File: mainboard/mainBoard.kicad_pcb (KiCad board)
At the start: 4 copper layers, 109.8 x 59.1 mm, 87 parts, among them IC1 TCAN3414DR, J1 XT60PW-M, J10 XT30U-M, J11 XT30U-M, J12 CAN Connector, J13 B2B-PH-K, J14 B2B-PH-K, J15 B2B-PH-K, J16 BM04B-SRSS-TB, J2 XT60PW-M, J20 BM04B-SRSS-TB, J21 B2B-PH_K, J22 Conn_01x02, J23 Jertson Header, J24 B2B-PH-K, J25 B2B-PH-K, J26 B2B-PH-K, J3 XT30PW-M, J4 XT30PW-M, J6 XT30U_M, J7 XT30U-M, J8 XT30U-M, J9 XT30U-M, Q1 FQD11P06TM, Q2 FQD11P06TM, U1 TPS565208, U2 TPS565208

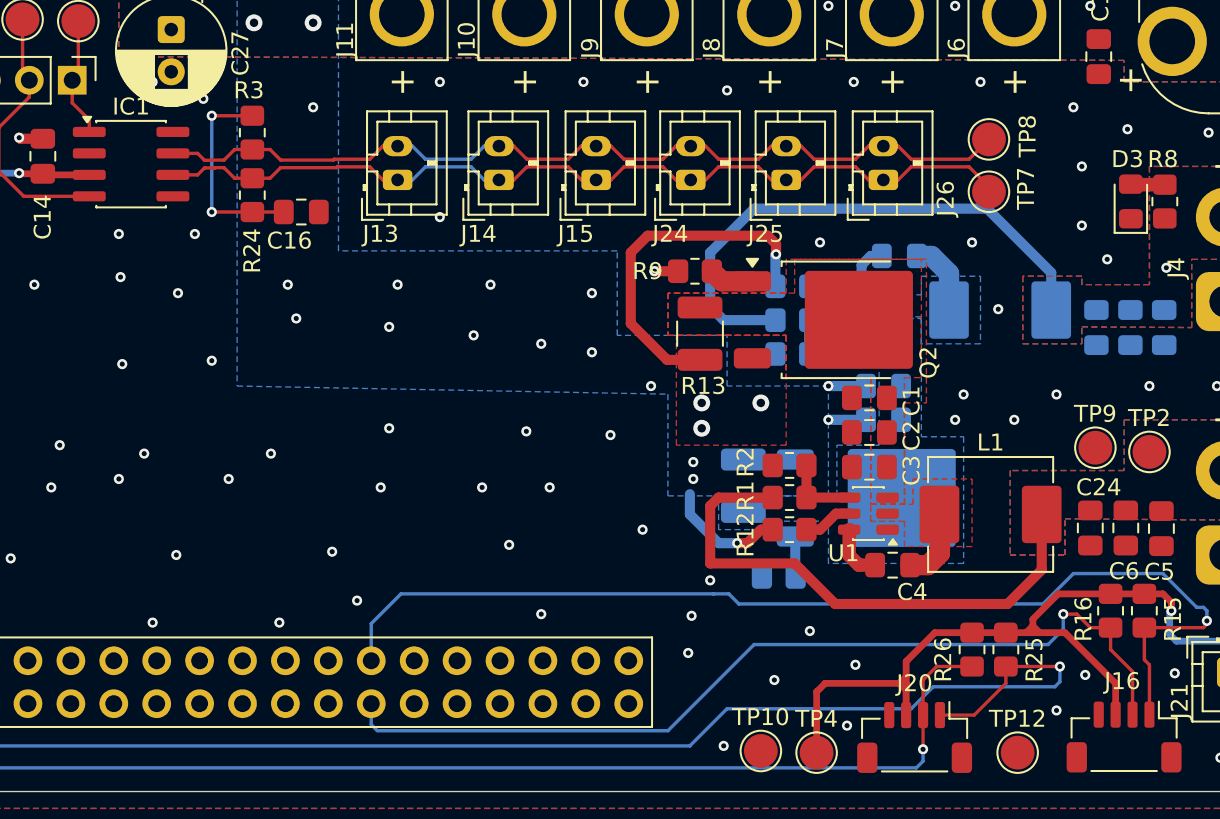
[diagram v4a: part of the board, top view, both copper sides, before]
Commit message: added tvs diode to baord (this was sylvester not nitin)
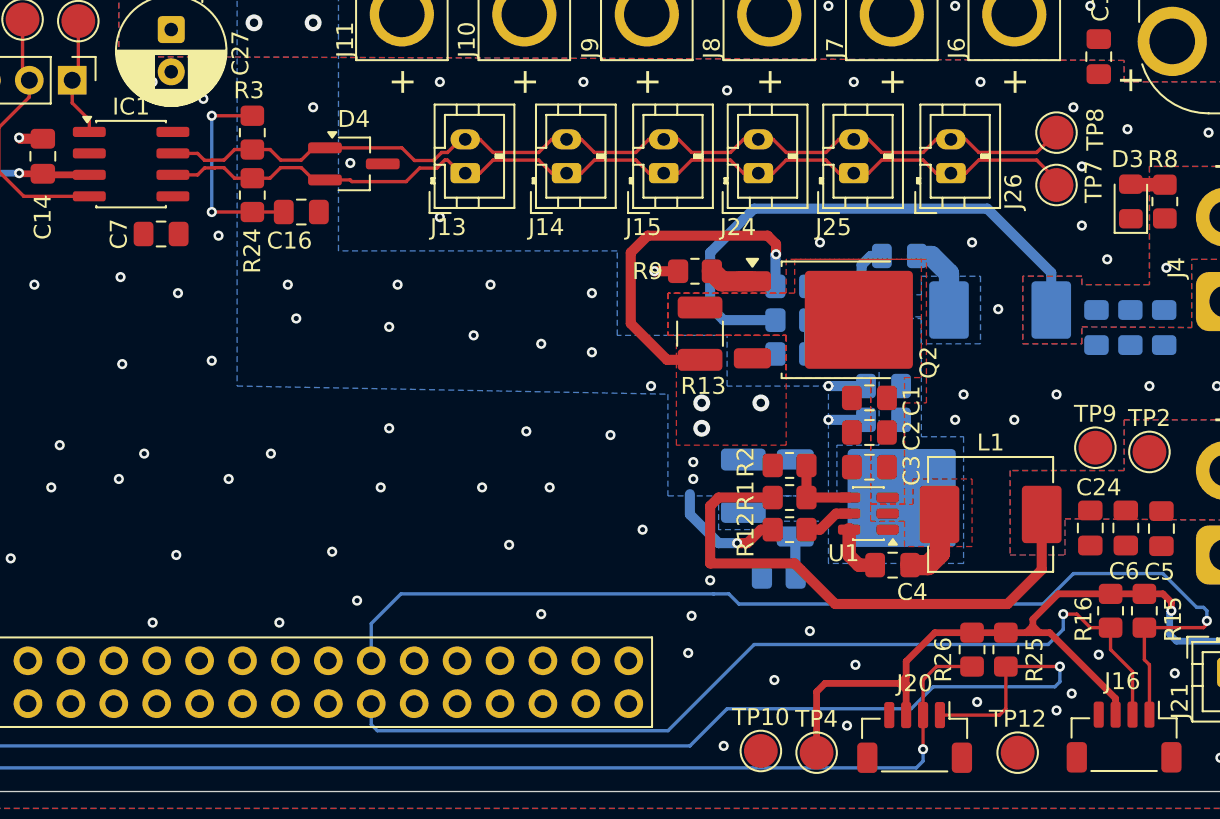
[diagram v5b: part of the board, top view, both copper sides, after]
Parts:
- added C7: 0.1uF, Capacitor_SMD:C_0805_2012Metric_Pad1.18x1.45mm_HandSolder, F.Cu at (84.1, 52.2)
- added D4: ESDCAN04-2BLY, Package_TO_SOT_SMD:TSOT-23_HandSoldering, F.Cu at (95.5, 48.1)
- moved J26 4.02 mm to (130.8, 48.6)
- moved TP7 4.02 mm to (137.1, 49.3)
- moved J13 4.02 mm to (102.1, 48.6)
- moved J14 4.02 mm to (108.1, 48.6)
- moved J15 4.02 mm to (113.8, 48.6)
- moved J24 4.02 mm to (119.4, 48.6)
- moved J25 4.02 mm to (125.1, 48.6)
- moved TP8 4.02 mm to (137.1, 46.2)
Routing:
- net CANN: track 53.7 -> 59.1 mm
- net CANP: track 53.4 -> 58.7 mm
- net SCL1: track 82.0 -> 82.9 mm
- net +3V3: track 249.6 -> 249.1 mm
- net GND: vias 146 -> 148
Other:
- board text added: "Nitin Shaker"
